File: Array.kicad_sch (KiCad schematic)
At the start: 0 parts

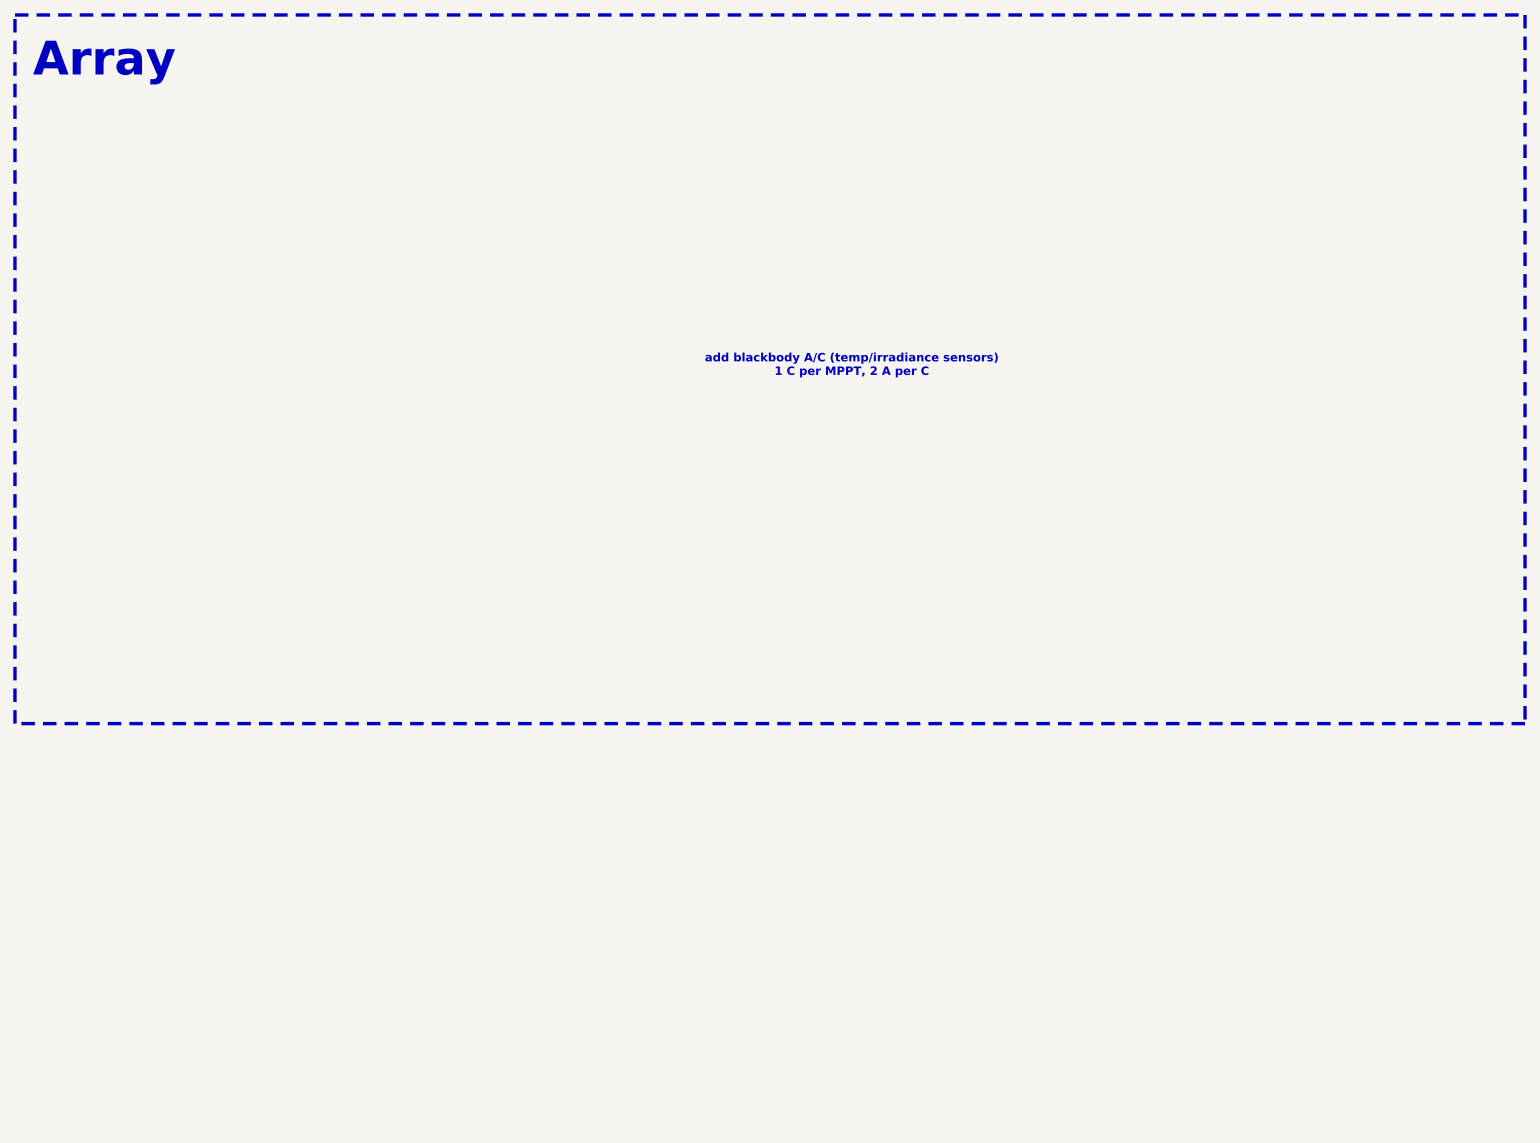
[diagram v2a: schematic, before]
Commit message: initial HV diagram changes
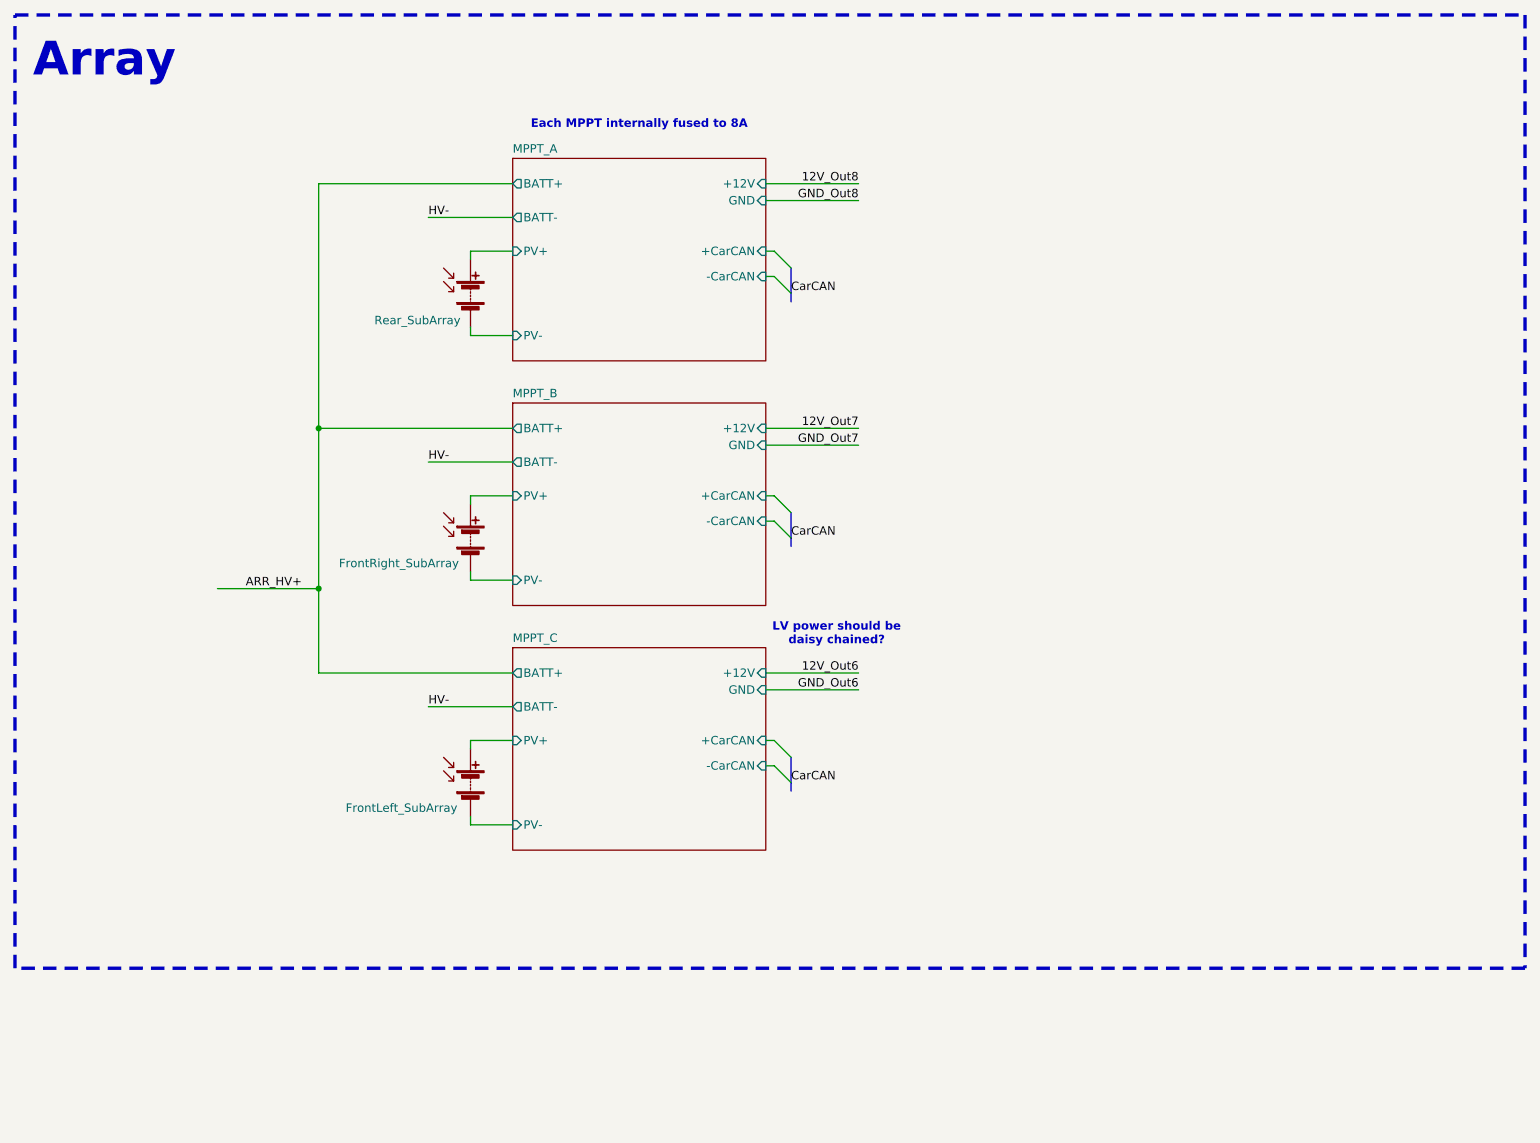
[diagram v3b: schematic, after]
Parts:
- added SC3: FrontLeft_SubArray, symbol Device:Solar_Cells
- added SC4: FrontRight_SubArray, symbol Device:Solar_Cells
- added SC5: Rear_SubArray, symbol Device:Solar_Cells
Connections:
- new net MPPT_A/PV+: SC5.1 (+)
- new net MPPT_A/PV-: SC5.2 (-)
- new net MPPT_B/PV+: SC4.1 (+)
- new net MPPT_B/PV-: SC4.2 (-)
- new net MPPT_C/PV+: SC3.1 (+)
- new net MPPT_C/PV-: SC3.2 (-)
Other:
- added sheet MPPT_A (MPPT.kicad_sch)
- added sheet MPPT_B (MPPT.kicad_sch)
- added sheet MPPT_C (MPPT.kicad_sch)
- note added: "Each MPPT internally fused to 8A"
- note added: "LV power should be daisy chained?"
- note removed: "add blackbody A/C (temp/irradiance sensors) 1 C per MPPT, 2 A per C"

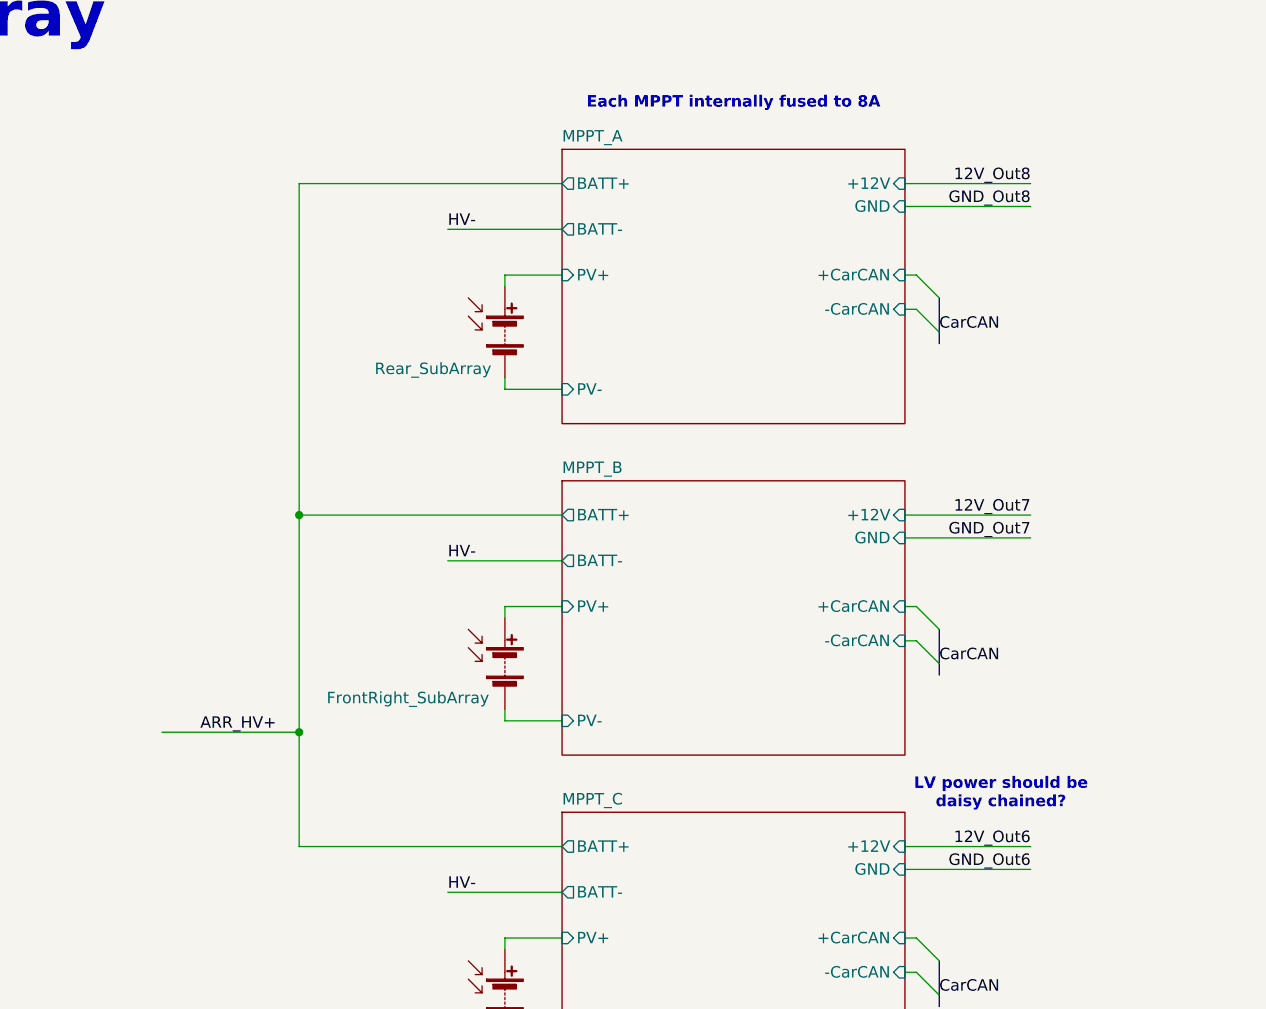
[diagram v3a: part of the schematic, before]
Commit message: reorganized top
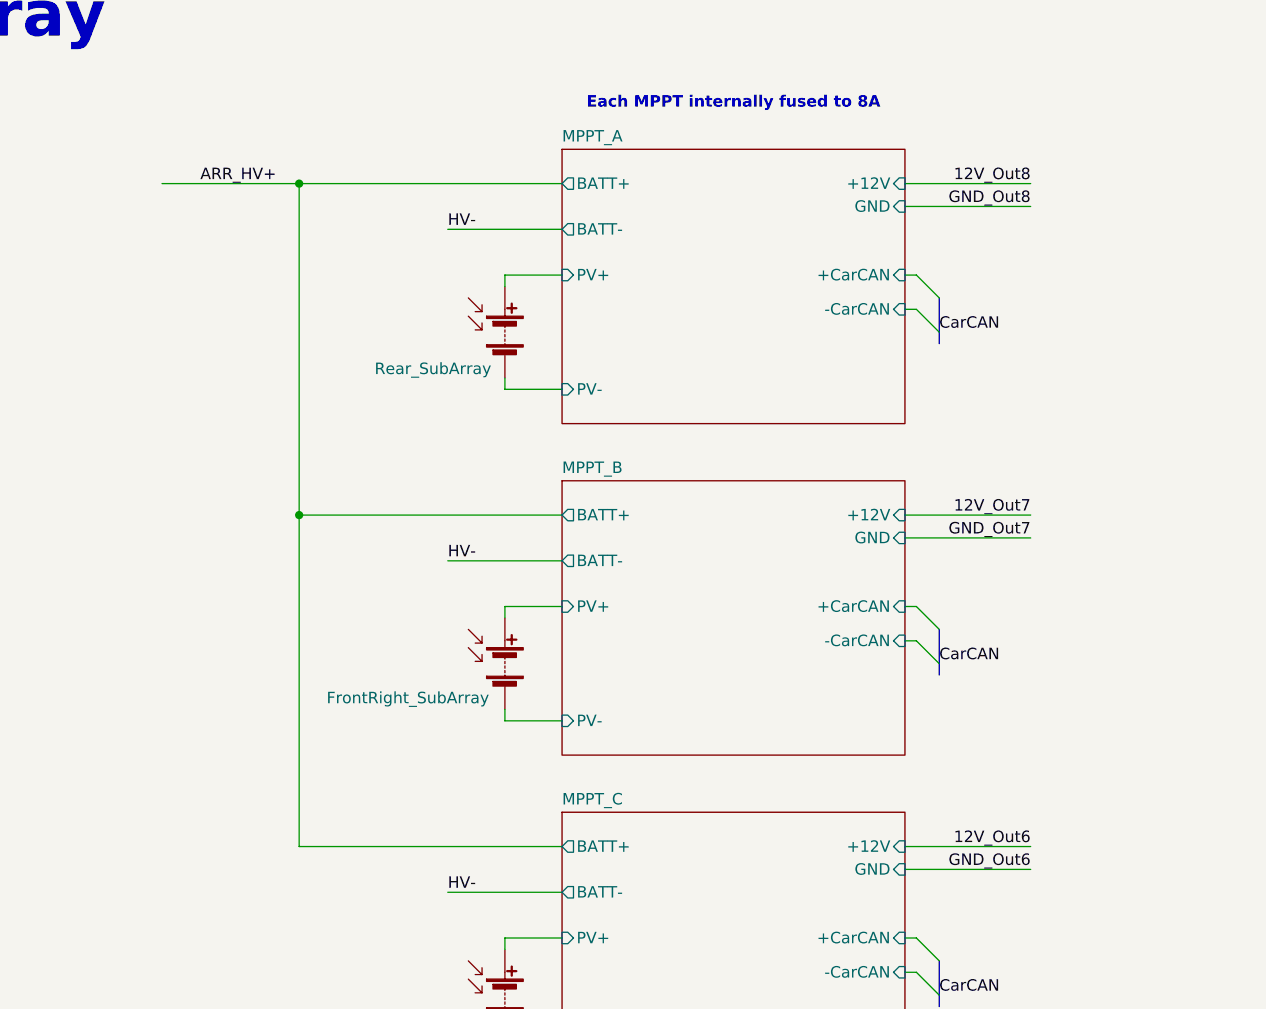
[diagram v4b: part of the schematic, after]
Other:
- note removed: "LV power should be daisy chained?"
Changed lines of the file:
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@@
-		)
-	)
-	(text "LV power should be\ndaisy chained?"
-		(exclude_from_sim no)
-		(at 141.478 110.998 0)
-		(effects
-			(font
-				(size 1.27 1.27)
-				(thickness 0.254)
-				(bold yes)
-				(color 255 0 0 1)
-			)
 		)
 	)
@@
 			)
 		)
+	)
+	(junction
+		(at 63.5 43.18)
+		(diameter 0)
+		(color 0 0 0 0)
 	)
 	(junction
@@
 		(color 0 0 0 0)
 	)
-	(junction
-		(at 63.5 104.14)
-		(diameter 0)
-		(color 0 0 0 0)
-	)
 	(bus_entry
 		(at 132.08 57.15)
@@
 	(wire
 		(pts
-			(xy 63.5 104.14) (xy 63.5 116.84)
+			(xy 130.81 93.98) (xy 132.08 93.98)
+		)
+		(stroke
+			(width 0)
+			(type default)
+		)
+	)
+	(wire
+		(pts
+			(xy 86.36 138.43) (xy 86.36 139.7)
+		)
+		(stroke
+			(width 0.381)
+			(type default)
+			(color 0 0 0 1)
+		)
+	)
+	(wire
+		(pts
+			(xy 130.81 116.84) (xy 144.78 116.84)
+		)
+		(stroke
+			(width 0)
+			(type default)
+			(color 254 0 0 1)
+		)
+	)
+	(bus
+		(pts
+			(xy 134.62 129.54) (xy 134.62 133.35)
+		)
+		(stroke
+			(width 0)
+			(type default)
+		)
+	)
+	(wire
+		(pts
+			(xy 92.71 102.87) (xy 86.36 102.87)
+		)
+		(stroke
+			(width 0.381)
+			(type default)
+			(color 0 0 0 1)
+		)
+	)
+	(wire
+		(pts
+			(xy 63.5 43.18) (xy 92.71 43.18)
 		)
 		(stroke
@@
 		)
 	)
-	(wire
-		(pts
-			(xy 130.81 93.98) (xy 132.08 93.98)
-		)
-		(stroke
-			(width 0)
-			(type default)
-		)
-	)
-	(wire
-		(pts
-			(xy 86.36 138.43) (xy 86.36 139.7)
-		)
-		(stroke
-			(width 0.381)
-			(type default)
-			(color 0 0 0 1)
-		)
-	)
-	(wire
-		(pts
-			(xy 130.81 116.84) (xy 144.78 116.84)
+	(bus
+		(pts
+			(xy 134.62 92.71) (xy 134.62 96.52)
+		)
+		(stroke
+			(width 0)
+			(type default)
+		)
+	)
+	(wire
+		(pts
+			(xy 130.81 130.81) (xy 132.08 130.81)
+		)
+		(stroke
+			(width 0)
+			(type default)
+		)
+	)
+	(wire
+		(pts
+			(xy 92.71 48.26) (xy 80.01 48.26)
+		)
+		(stroke
+			(width 0.381)
+			(type default)
+			(color 254 137 0 1)
+		)
+	)
+	(wire
+		(pts
+			(xy 130.81 43.18) (xy 144.78 43.18)
 		)
 		(stroke
@@
 		)
 	)
+	(wire
+		(pts
+			(xy 130.81 127) (xy 132.08 127)
+		)
+		(stroke
+			(width 0)
+			(type default)
+		)
+	)
 	(bus
 		(pts
-			(xy 134.62 129.54) (xy 134.62 133.35)
-		)
-		(stroke
-			(width 0)
-			(type default)
-		)
-	)
-	(wire
-		(pts
-			(xy 92.71 102.87) (xy 86.36 102.87)
-		)
-		(stroke
-			(width 0.381)
-			(type default)
-			(color 0 0 0 1)
-		)
-	)
-	(wire
-		(pts
-			(xy 63.5 43.18) (xy 92.71 43.18)
+			(xy 134.62 133.35) (xy 134.62 134.62)
+		)
+		(stroke
+			(width 0)
+			(type default)
+		)
+	)
+	(wire
+		(pts
+			(xy 63.5 80.01) (xy 63.5 116.84)
 		)
 		(stroke
@@
 		)
 	)
-	(bus
-		(pts
-			(xy 134.62 92.71) (xy 134.62 96.52)
-		)
-		(stroke
-			(width 0)
-			(type default)
-		)
-	)
-	(wire
-		(pts
-			(xy 130.81 130.81) (xy 132.08 130.81)
-		)
-		(stroke
-			(width 0)
-			(type default)
-		)
-	)
-	(wire
-		(pts
-			(xy 92.71 48.26) (xy 80.01 48.26)
+	(wire
+		(pts
+			(xy 86.36 127) (xy 92.71 127)
+		)
+		(stroke
+			(width 0.381)
+			(type default)
+			(color 254 0 0 1)
+		)
+	)
+	(wire
+		(pts
+			(xy 92.71 121.92) (xy 80.01 121.92)
 		)
 		(stroke
@@
 	(wire
 		(pts
-			(xy 130.81 43.18) (xy 144.78 43.18)
-		)
-		(stroke
-			(width 0)
+			(xy 86.36 53.34) (xy 92.71 53.34)
+		)
+		(stroke
+			(width 0.381)
 			(type default)
 			(color 254 0 0 1)
@@
 	(wire
 		(pts
-			(xy 130.81 127) (xy 132.08 127)
-		)
-		(stroke
-			(width 0)
-			(type default)
-		)
-	)
-	(bus
-		(pts
-			(xy 134.62 133.35) (xy 134.62 134.62)
-		)
-		(stroke
-			(width 0)
-			(type default)
-		)
-	)
-	(wire
-		(pts
-			(xy 63.5 80.01) (xy 63.5 104.14)
-		)
-		(stroke
-			(width 0.381)
-			(type default)
-			(color 254 137 0 1)
-		)
-	)
-	(wire
-		(pts
-			(xy 86.36 127) (xy 92.71 127)
-		)
-		(stroke
-			(width 0.381)
-			(type default)
-			(color 254 0 0 1)
-		)
-	)
-	(wire
-		(pts
-			(xy 92.71 121.92) (xy 80.01 121.92)
-		)
-		(stroke
-			(width 0.381)
-			(type default)
-			(color 254 137 0 1)
-		)
-	)
-	(wire
-		(pts
-			(xy 86.36 53.34) (xy 92.71 53.34)
-		)
-		(stroke
-			(width 0.381)
-			(type default)
-			(color 254 0 0 1)
-		)
-	)
-	(wire
-		(pts
-			(xy 63.5 104.14) (xy 48.26 104.14)
+			(xy 63.5 43.18) (xy 48.26 43.18)
 		)
 		(stroke
@@
 	)
 	(label "ARR_HV+"
-		(at 60.96 104.14 180)
+		(at 60.96 43.18 180)
 		(effects
 			(font
@@
 					(unit 1)
 				)
-				(path "/7dc721ab-4b7a-42e7-8fa4-f406a2ddcd46/e094edde-623e-4790-8114-bc89a5278135"
-					(reference "SC6")
-					(unit 1)
-				)
 			)
 		)
@@
 					(unit 1)
 				)
-				(path "/7dc721ab-4b7a-42e7-8fa4-f406a2ddcd46/e094edde-623e-4790-8114-bc89a5278135"
-					(reference "SC7")
-					(unit 1)
-				)
 			)
 		)
@@
 					(unit 1)
 				)
-				(path "/7dc721ab-4b7a-42e7-8fa4-f406a2ddcd46/e094edde-623e-4790-8114-bc89a5278135"
-					(reference "SC8")
-					(unit 1)
-				)
 			)
 		)
@@
 					(page "51")
 				)
-				(path "/7dc721ab-4b7a-42e7-8fa4-f406a2ddcd46/e094edde-623e-4790-8114-bc89a5278135"
-					(page "55")
-				)
 			)
 		)
@@
 					(page "40")
 				)
-				(path "/7dc721ab-4b7a-42e7-8fa4-f406a2ddcd46/e094edde-623e-4790-8114-bc89a5278135"
-					(page "53")
-				)
 			)
 		)
@@
 					(page "49")
 				)
-				(path "/7dc721ab-4b7a-42e7-8fa4-f406a2ddcd46/e094edde-623e-4790-8114-bc89a5278135"
-					(page "54")
-				)
-			)
+			)

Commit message: array stuff
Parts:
- removed SC3: FrontLeft_SubArray, symbol Device:Solar_Cells
- removed SC4: FrontRight_SubArray, symbol Device:Solar_Cells
- removed SC5: Rear_SubArray, symbol Device:Solar_Cells
- added U13, U14, U7: BlackbodyA, symbol lib:BlackbodyA
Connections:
- net 12V_Out8: now also U13. (CAN-), U14. (CAN-), U7. (CAN-)
- net GND_Out8: now also U13. (CAN-), U14. (CAN-), U7. (CAN-)
- new net Array/ARR_A_I2C: U7. (CAN-)
- new net Array/ARR_B_I2C: U13. (CAN-)
- new net Array/ARR_C_I2C: U14. (CAN-)
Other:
- added sheet Array (Array2.kicad_sch)
- note added: "A"
- note added: "B"
- note added: "C"
- note removed: "Array"
